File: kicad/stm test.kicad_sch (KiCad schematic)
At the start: 2 parts, among them U101 MCP23008-xP

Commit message: womp
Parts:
- removed U101: MCP23008-xP, Package_DIP:DIP-18_W7.62mm_Socket_LongPads, symbol Interface_Expansion:MCP23008-xP
- added A102: Pololu_Breakout_A4988, Module:Pololu_Breakout-16_15.2x20.3mm, symbol Driver_Motor:Pololu_Breakout_A4988
- added C101, C103, C402: 220n, Capacitor_SMD:C_0805_2012Metric_Pad1.18x1.45mm_HandSolder, symbol Device:C_Small
- added C102, C401: 10u, Capacitor_SMD:C_1206_3216Metric_Pad1.33x1.80mm_HandSolder, symbol Device:C_Small
- added D104: ES1D, Diode_SMD:D_SMA, symbol Device:D_Schottky_Small
- added F101, F24: 1.5A, Resistor_THT:R_Bare_Metal_Element_L21.3mm_W4.8mm_P20.30mm, symbol Device:Fuse
- added J101: pwr, symbol Connector:Conn_01x02_Pin
- added J102: conv motor, TerminalBlock:TerminalBlock_Xinya_XY308-2.54-2P_1x02_P2.54mm_Horizontal, symbol Connector:Conn_01x02_Pin
- added J103: stepper, TerminalBlock:TerminalBlock_Xinya_XY308-2.54-4P_1x04_P2.54mm_Horizontal, symbol Connector:Conn_01x04_Pin
- added J104: led_driver, TerminalBlock:TerminalBlock_Xinya_XY308-2.54-4P_1x04_P2.54mm_Horizontal, symbol Connector:Conn_01x04_Pin
- added J106: beam sensor, TerminalBlock:TerminalBlock_Xinya_XY308-2.54-3P_1x03_P2.54mm_Horizontal, symbol Connector:Conn_01x03_Pin
- added R101: 432k, Resistor_SMD:R_1206_3216Metric_Pad1.30x1.75mm_HandSolder, symbol Device:R_Small_US
- added R102: 22.1k, Resistor_SMD:R_0805_2012Metric_Pad1.20x1.40mm_HandSolder, symbol Device:R_Small_US
- added R408: 49.9k, Resistor_SMD:R_0805_2012Metric_Pad1.20x1.40mm_HandSolder, symbol Device:R_Small_US
- added R411: 38.3k, Resistor_SMD:R_0805_2012Metric_Pad1.20x1.40mm_HandSolder, symbol Device:R_Small_US
- added U101: MCP23S08-xP, Package_DIP:DIP-18_W7.62mm, symbol local:MCP23S08-xP
- added U102: TPS26600PWPR, local:PWP0016H_M, symbol local:TPS26600PWPR
- added U103: MIC5014YM, Package_SO:SOIC-8_3.9x4.9mm_P1.27mm, symbol local:MIC5014
- added U406: IPD14N06, Package_TO_SOT_SMD:TO-252-2, symbol zzLocalLibrary:IPD14N06S2
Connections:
- net conv_M_pwm: now reaches A101.10 (A1)
- net conv_M_pwm: now also U103.2 (ctrl_input)
- net spiA.sclk: now reaches A101.19 (D4)
- net spiA.sclk: now also U101.1 (SCK)
- net spiA.miso: now reaches A101.20 (D5)
- net spiA.miso: now also U101.2 (SI)
- net spiA.mosi: now reaches A101.21 (D6)
- net spiA.mosi: now also U101.3 (SO)
- net stepper.step: now reaches A101.22 (D7)
- net stepper.step: now also A102.15 (STEP)
- net GND: now reaches A101.29 (GND)
- net GND: now also A101.6 (GND), A101.7 (GND), A102.1 (GND), A102.7 (GND), C101.2, C102.2, C103.2, C401.2, C402.2, D104.2 (A), J101.2 (Pin_2), J104.3 (Pin_3), J106.3 (Pin_3), R102.1, R408.1, U101.4 (A1), U101.5 (A0), U101.9 (VSS), U102.17 (PAD), U102.8 (RTN), U102.9 (GND), U103.4 (gnd)
- net +3V3: now reaches A101.4 (3V3)
- net +3V3: now also A102.2 (VDD), U101.18 (VDD)
- net +5V: now reaches A101.5 (+5V)
- net +12V: now reaches A101.8 (VIN)
- net +12V: now also C101.1, C401.1, J104.4 (Pin_4), U102.15 (OUT), U102.16 (OUT)
- new net: A102.3 (1B), J103.1 (Pin_1)
- new net: A102.4 (1A), J103.2 (Pin_2)
- new net: A102.5 (2A), J103.3 (Pin_3)
- new net: A102.6 (2B), J103.4 (Pin_4)
- new net: R102.2, U102.11 (ILIM)
- new net: R408.2, R411.1, U102.5 (OVP)
- new net: A102.8 (VMOT), C103.1, F101.2
- new net: C102.1, F24.2, U103.1 (V+), U406.2 (D)
- new net: R101.1, R411.2, U102.3 (UVLO)
- new net: U103.5 (gate), U406.1 (G)
- new net LV+: C402.1, F101.1, J101.1 (Pin_1), R101.2, U102.1 (IN), U102.2 (IN)
- new net bs.enable: J106.2 (Pin_2), U101.10 (GP0)
- new net bs.sense: J106.1 (Pin_1), U101.11 (GP1)
- new net conv_M+: D104.1 (K), J102.2 (Pin_2), U103.3 (source), U406.3 (S)
- new net conv_V+: F24.1, J102.1 (Pin_1)
- new net ledD_clk: J104.1 (Pin_1)
- new net ledD_da: J104.2 (Pin_2)
- new net mcp.int: U101.8 (INT)
- new net mcp.rst_n: U101.6 (RST_N)
- new net spiA.cs_MCP: U101.7 (CS_N)
- new net stepper.dir: A102.16 (DIR)
- new net stepper.enable_n: A102.9 (~{ENABLE})
- new net stepper.ms1: A102.10 (MS1)
- new net stepper.ms2: A102.11 (MS2)
- new net stepper.ms3: A102.12 (MS3)
- new net stepper.reset_n: A102.13 (~{RESET})
- new net stepper.sleep_n: A102.14 (~{SLEEP})
- no-connect marks 0 -> 13
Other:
- note added: "TODO:assign to convient gpio"
- note added: "[-60,60]V tollerant [7,12]V working"
- note removed: "- 3 pin XH. pwr, gnd, pwm - 5v in - 2 pin XH. led driver bus"
- moved on the sheet: A101

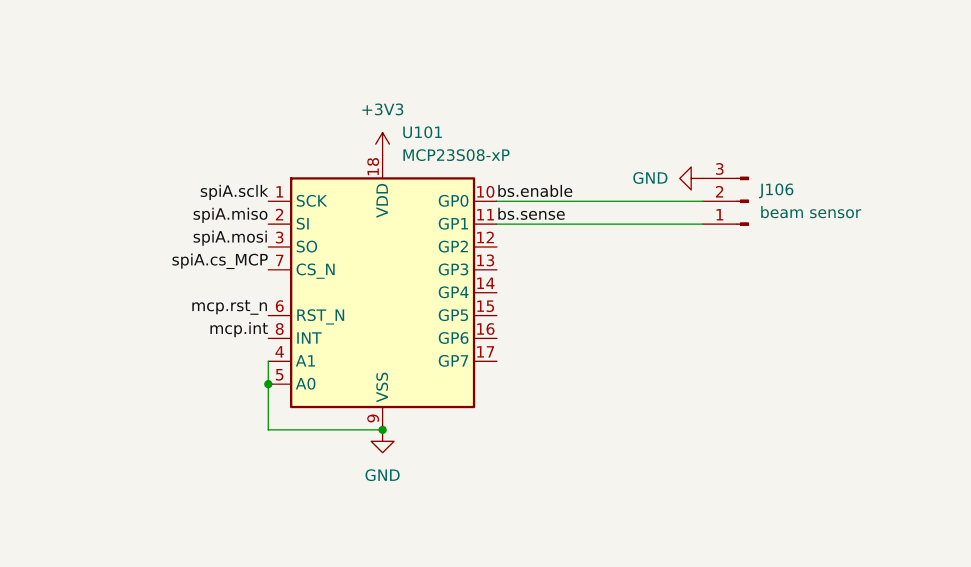
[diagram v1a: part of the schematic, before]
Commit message: corrected spi wiring error
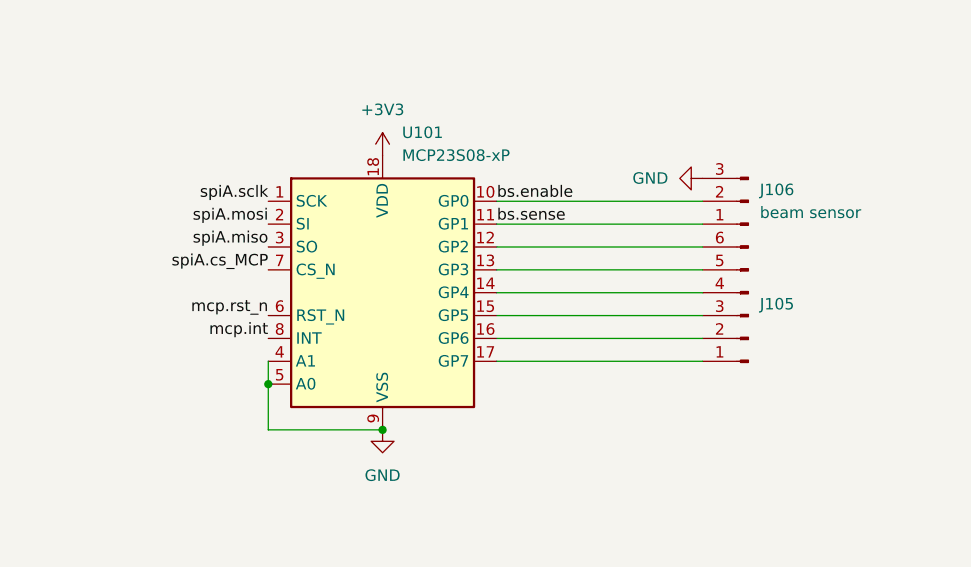
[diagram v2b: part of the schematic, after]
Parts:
- added J105: Conn_01x06_Pin, Connector_PinHeader_2.54mm:PinHeader_1x06_P2.54mm_Vertical, symbol Connector:Conn_01x06_Pin
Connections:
- net spiA.miso: now also U101.3 (SO); no longer U101.2 (SI)
- net spiA.mosi: now also U101.2 (SI); no longer U101.3 (SO)
- net at U101.12 (GP2): now also J105.6 (Pin_6)
- net at U101.13 (GP3): now also J105.5 (Pin_5)
- net at U101.14 (GP4): now also J105.4 (Pin_4)
- net at U101.15 (GP5): now also J105.3 (Pin_3)
- net at U101.16 (GP6): now also J105.2 (Pin_2)
- net at U101.17 (GP7): now also J105.1 (Pin_1)
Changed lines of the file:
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@@
+	(wire
+		(pts
+			(xy 240.03 127) (xy 217.17 127)
+		)
+		(stroke
+			(width 0)
+			(type default)
+		)
+	)
 	(wire
 		(pts
@@
 	(wire
 		(pts
+			(xy 240.03 132.08) (xy 217.17 132.08)
+		)
+		(stroke
+			(width 0)
+			(type default)
+		)
+	)
+	(wire
+		(pts
 			(xy 100.33 24.13) (xy 101.6 24.13)
 		)
@@
 	(wire
 		(pts
+			(xy 240.03 134.62) (xy 217.17 134.62)
+		)
+		(stroke
+			(width 0)
+			(type default)
+		)
+	)
+	(wire
+		(pts
 			(xy 35.56 137.16) (xy 58.42 137.16)
 		)
@@
 	(wire
 		(pts
+			(xy 240.03 137.16) (xy 217.17 137.16)
+		)
+		(stroke
+			(width 0)
+			(type default)
+		)
+	)
+	(wire
+		(pts
 			(xy 100.33 26.67) (xy 101.6 26.67)
 		)
@@
 	(wire
 		(pts
+			(xy 240.03 124.46) (xy 217.17 124.46)
+		)
+		(stroke
+			(width 0)
+			(type default)
+		)
+	)
+	(wire
+		(pts
 			(xy 55.88 85.09) (xy 55.88 100.33)
 		)
@@
 		(pts
 			(xy 57.15 116.84) (xy 66.04 116.84)
+		)
+		(stroke
+			(width 0)
+			(type default)
+		)
+	)
+	(wire
+		(pts
+			(xy 240.03 129.54) (xy 217.17 129.54)
 		)
 		(stroke
@@
 	)
 	(label "spiA.miso"
-		(at 191.77 121.92 180)
+		(at 191.77 124.46 180)
 		(effects
 			(font
@@
 	)
 	(label "spiA.mosi"
-		(at 191.77 124.46 180)
+		(at 191.77 121.92 180)
 		(effects
 			(font
@@
 					(unit 1)
 				)
+			)
+		)
+	)
+	(symbol
+		(lib_id "Connector:Conn_01x06_Pin")
+		(at 245.11 132.08 180)
+		(unit 1)
+		(exclude_from_sim no)
+		(in_bom yes)
+		(on_board yes)
+		(dnp no)
+		(fields_autoplaced yes)
+		(property "Reference" "J105"
+			(at 246.38 130.8099 0)
+			(effects
+				(font
+					(size 1.27 1.27)
+				)
+				(justify right)
+			)
+		)
+		(property "Value" "Conn_01x06_Pin"
+			(at 246.38 132.0799 0)
+			(effects
+				(font
+					(size 1.27 1.27)
+				)
+				(justify right)
+				(hide yes)
+			)
+		)
+		(property "Footprint" "Connector_PinHeader_2.54mm:PinHeader_1x06_P2.54mm_Vertical"
+			(at 245.11 132.08 0)
+			(effects
+				(font
+					(size 1.27 1.27)
+				)
+				(hide yes)
+			)
+		)
+		(property "Datasheet" "~"
+			(at 245.11 132.08 0)
+			(effects
+				(font
+					(size 1.27 1.27)
+				)
+				(hide yes)
+			)
+		)
+		(property "Description" "Generic connector, single row, 01x06, script generated"
+			(at 245.11 132.08 0)
+			(effects
+				(font
+					(size 1.27 1.27)
+				)
+				(hide yes)
+			)
+		)
+		(pin "2"
+		)
+		(pin "3"
+		)
+		(pin "5"
+		)
+		(pin "6"
+		)
+		(pin "1"
+		)
+		(pin "4"
+		)
+		(instances
+			(project ""
+				(path "/87cc8d3e-d630-413b-88b8-457ea5f51541"
+					(reference "J105")
+					(unit 1)
+				)

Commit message: i fugged up
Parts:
- removed C103: 220n, Capacitor_SMD:C_0805_2012Metric_Pad1.18x1.45mm_HandSolder, symbol Device:C_Small
- removed F101: 1.5A, Resistor_THT:R_Bare_Metal_Element_L21.3mm_W4.8mm_P20.30mm, symbol Device:Fuse
- removed R102: 22.1k, Resistor_SMD:R_0805_2012Metric_Pad1.20x1.40mm_HandSolder, symbol Device:R_Small_US
- added C2: 10u, Capacitor_SMD:C_1206_3216Metric_Pad1.33x1.80mm_HandSolder, symbol Device:C_Small
- added F1: 1.5A, Resistor_THT:R_Axial_DIN0207_L6.3mm_D2.5mm_P7.62mm_Horizontal, symbol Device:Fuse
- F2: renamed from F24; footprint Resistor_THT:R_Bare_Metal_Element_L21.3mm_W4.8mm_P20.30mm -> Resistor_THT:R_Axial_DIN0207_L6.3mm_D2.5mm_P7.62mm_Horizontal
- J1: renamed from J101; footprint (none) -> TerminalBlock:TerminalBlock_Xinya_XY308-2.54-2P_1x02_P2.54mm_Horizontal
- renumbered A102 to A1, A101 to A2, C402 to C1, C401 to C3, C102 to C4, C101 to C5, D104 to D1, J104 to J2, J102 to J3, J103 to J4, J106 to J5, J105 to J6, R101 to R1, R411 to R2, R408 to R3, U406 to U1, U102 to U2, U103 to U3, U101 to U4
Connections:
- net +12V: now also A1.8 (VMOT), J2.2 (Pin_2), C2.1; no longer J2.4 (Pin_4)
- net GND: now also J2.1 (Pin_1), J5.1 (Pin_1), C2.2; no longer J2.3 (Pin_3), J5.3 (Pin_3)
- net LV+: now also F1.1; no longer C1.1, R1.2, U2.1 (IN), U2.2 (IN)
- net bs.sense: now also J5.3 (Pin_3); no longer J5.1 (Pin_1)
- net ledD_clk: now also A2.15 (D0/RX), J2.3 (Pin_3); no longer J2.1 (Pin_1)
- net ledD_da: now also A2.16 (D1/TX), J2.4 (Pin_4); no longer J2.2 (Pin_2)
- net mcp.int: now also A2.28 (D13)
- net mcp.rst_n: now also A2.32 (SCL/A5)
- net spiA.cs_MCP: now also A2.31 (SDA/A4)
- net stepper.dir: now also A2.18 (D3)
- net stepper.enable_n: now also A2.27 (D12)
- net stepper.ms1: now also A2.26 (D11)
- net stepper.ms2: now also A2.25 (D10)
- net stepper.ms3: now also A2.24 (D9)
- net stepper.reset_n: now also A2.23 (D8)
- net stepper.sleep_n: now also A2.17 (D2)
- new net: C1.1, F1.2, R1.2, U2.1 (IN), U2.2 (IN)
- no-connect marks 13 -> 14
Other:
- moved on the sheet: J5

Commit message: test pin
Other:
- note removed: "[-60,60]V tollerant [7,12]V working"
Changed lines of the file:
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@@
 	(generator_version "9.0")
 	(paper "A4")
-	(text "[-60,60]V tollerant\n[7,12]V working"
-		(exclude_from_sim no)
-		(at 35.306 19.304 0)
-		(effects
-			(font
-				(size 1.27 1.27)
-				(color 194 0 194 1)
-			)
-			(justify left top)
-		)
-	)
 	(text "TODO:assign to convient gpio"
 		(exclude_from_sim no)
